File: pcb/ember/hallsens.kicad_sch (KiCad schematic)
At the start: 68 parts, among them IC1 CD4051BM96, IC2 CD4051BM96, IC3 CD4051BM96, IC4 CD4051BM96, U10 Hall_Sensor, U11 Hall_Sensor, U12 Hall_Sensor, U13 Hall_Sensor, U14 Hall_Sensor, U15 Hall_Sensor, U16 Hall_Sensor, U17 Hall_Sensor, U18 Hall_Sensor, U19 Hall_Sensor, U2 Hall_Sensor, U20 Hall_Sensor, U21 Hall_Sensor, U22 Hall_Sensor, U23 Hall_Sensor, U24 Hall_Sensor, U25 Hall_Sensor, U26 Hall_Sensor, U27 Hall_Sensor, U28 Hall_Sensor, U29 Hall_Sensor, U3 Hall_Sensor, U30 Hall_Sensor, U31 Hall_Sensor, U32 Hall_Sensor, U33 Hall_Sensor, U4 Hall_Sensor, U5 Hall_Sensor, U6 Hall_Sensor, U7 Hall_Sensor, U8 Hall_Sensor, U9 Hall_Sensor

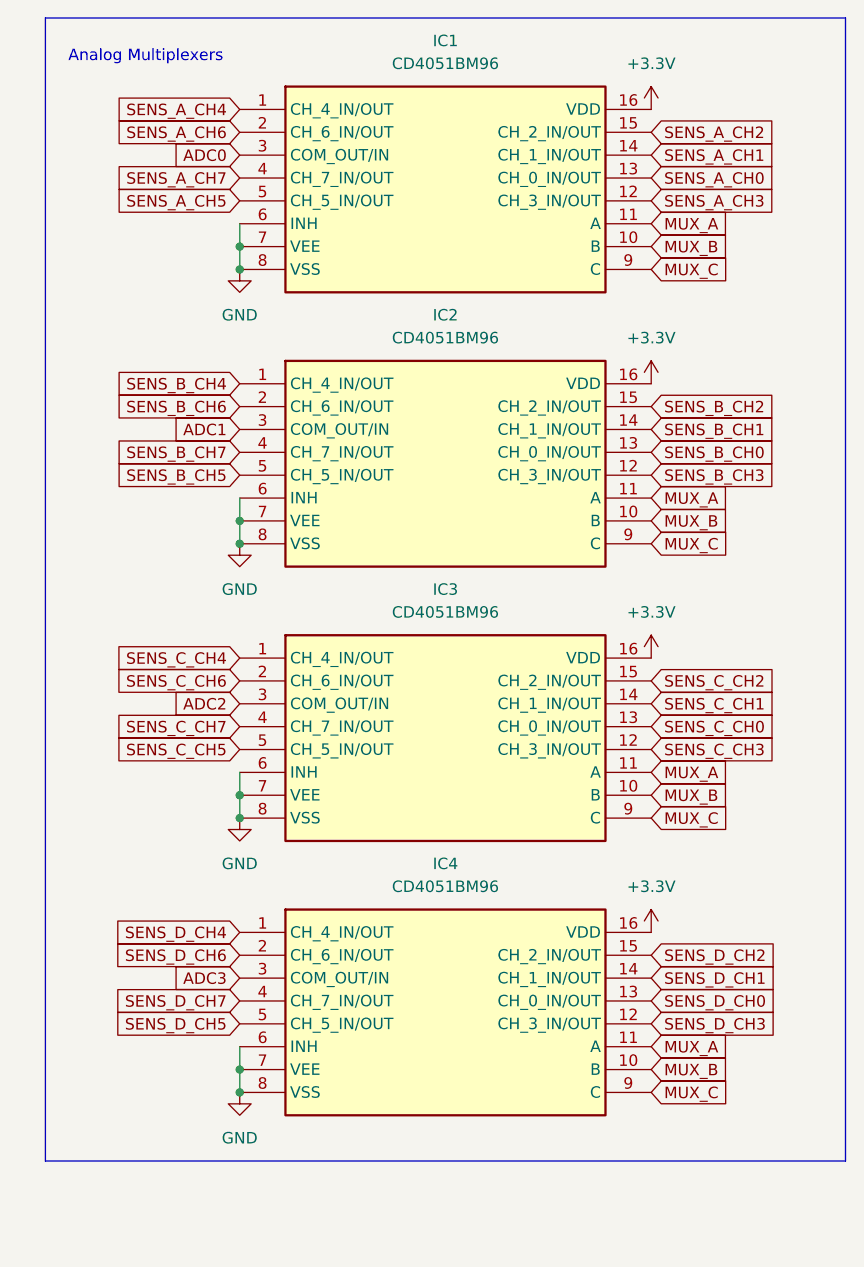
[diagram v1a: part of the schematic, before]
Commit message: :sparkles: add eeprom
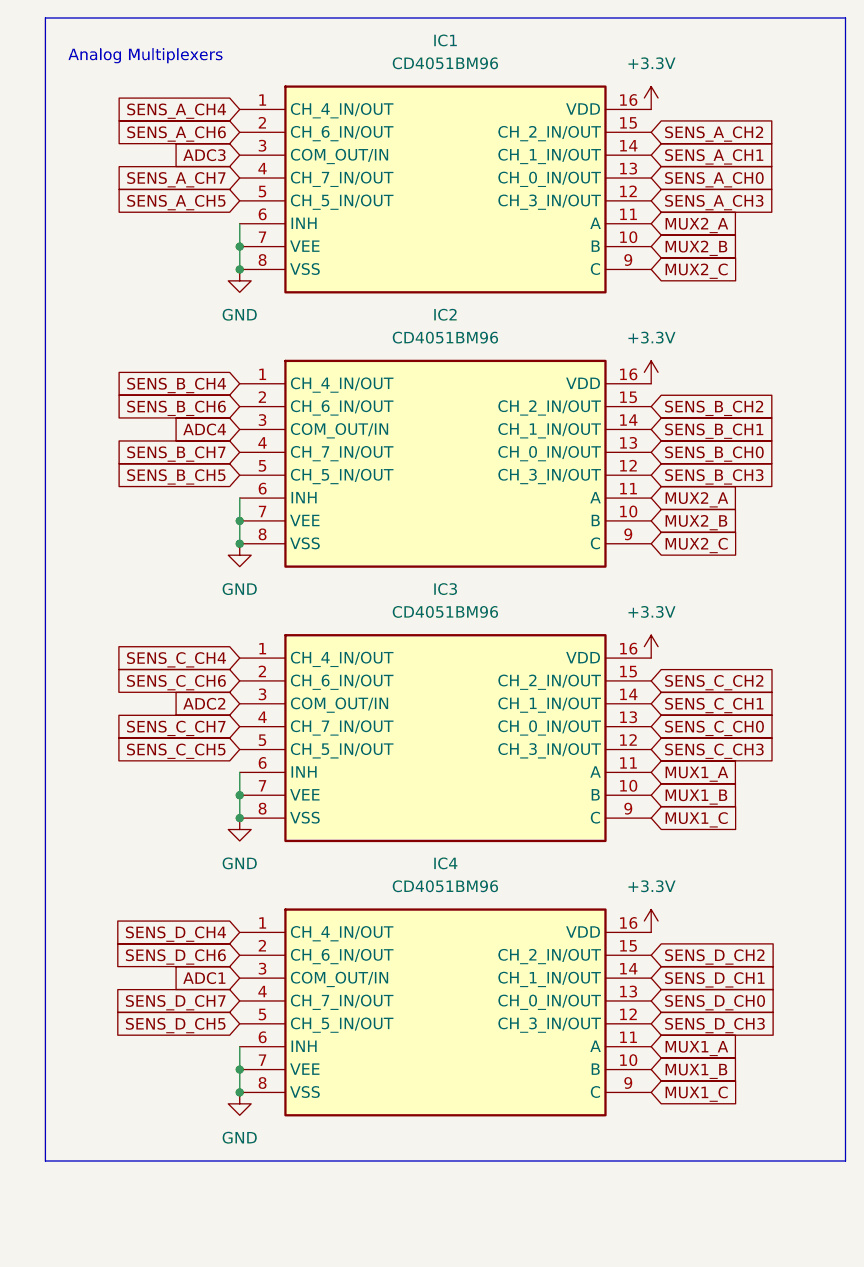
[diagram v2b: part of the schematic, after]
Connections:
- net ADC0 is gone; now on net ADC3: IC1.3 (COM_OUT/IN)
- net ADC1: now also IC4.3 (COM_OUT/IN); no longer IC2.3 (COM_OUT/IN)
- net ADC3: no longer IC4.3 (COM_OUT/IN)
- net MUX_A renamed MUX1_A
- net MUX1_A: no longer IC1.11 (A), IC2.11 (A)
- net MUX_B renamed MUX1_B
- net MUX1_B: no longer IC1.10 (B), IC2.10 (B)
- net MUX_C renamed MUX1_C
- net MUX1_C: no longer IC1.9 (C), IC2.9 (C)
- new net ADC4: IC2.3 (COM_OUT/IN)
- new net MUX2_A: IC1.11 (A), IC2.11 (A)
- new net MUX2_B: IC1.10 (B), IC2.10 (B)
- new net MUX2_C: IC1.9 (C), IC2.9 (C)
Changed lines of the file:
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@@
     )
   )
-  (global_label "MUX_C" (shape input) (at 237.49 114.3 0) (fields_autoplaced)
-    (effects (font (size 1.27 1.27)) (justify left))
-    (property "Intersheetrefs" "${INTERSHEET_REFS}" (at 246.7042 114.3 0)
-      (effects (font (size 1.27 1.27)) (justify left) hide)
-    )
-  )
-  (global_label "MUX_C" (shape input) (at 237.49 53.34 0) (fields_autoplaced)
-    (effects (font (size 1.27 1.27)) (justify left))
-    (property "Intersheetrefs" "${INTERSHEET_REFS}" (at 246.7042 53.34 0)
+  (global_label "MUX1_A" (shape input) (at 237.49 139.7 0) (fields_autoplaced)
+    (effects (font (size 1.27 1.27)) (justify left))
+    (property "Intersheetrefs" "${INTERSHEET_REFS}" (at 247.7323 139.7 0)
+      (effects (font (size 1.27 1.27)) (justify left) hide)
+    )
+  )
+  (global_label "MUX1_B" (shape input) (at 237.49 142.24 0) (fields_autoplaced)
+    (effects (font (size 1.27 1.27)) (justify left))
+    (property "Intersheetrefs" "${INTERSHEET_REFS}" (at 247.9137 142.24 0)
+      (effects (font (size 1.27 1.27)) (justify left) hide)
+    )
+  )
+  (global_label "MUX1_C" (shape input) (at 237.49 114.3 0) (fields_autoplaced)
+    (effects (font (size 1.27 1.27)) (justify left))
+    (property "Intersheetrefs" "${INTERSHEET_REFS}" (at 247.9137 114.3 0)
+      (effects (font (size 1.27 1.27)) (justify left) hide)
+    )
+  )
+  (global_label "MUX2_C" (shape input) (at 237.49 53.34 0) (fields_autoplaced)
+    (effects (font (size 1.27 1.27)) (justify left))
+    (property "Intersheetrefs" "${INTERSHEET_REFS}" (at 247.9137 53.34 0)
       (effects (font (size 1.27 1.27)) (justify left) hide)
     )
@@
     )
   )
-  (global_label "MUX_A" (shape input) (at 237.49 109.22 0) (fields_autoplaced)
-    (effects (font (size 1.27 1.27)) (justify left))
-    (property "Intersheetrefs" "${INTERSHEET_REFS}" (at 246.5228 109.22 0)
-      (effects (font (size 1.27 1.27)) (justify left) hide)
-    )
-  )
-  (global_label "MUX_B" (shape input) (at 237.49 81.28 0) (fields_autoplaced)
-    (effects (font (size 1.27 1.27)) (justify left))
-    (property "Intersheetrefs" "${INTERSHEET_REFS}" (at 246.7042 81.28 0)
+  (global_label "MUX1_A" (shape input) (at 237.49 109.22 0) (fields_autoplaced)
+    (effects (font (size 1.27 1.27)) (justify left))
+    (property "Intersheetrefs" "${INTERSHEET_REFS}" (at 247.7323 109.22 0)
       (effects (font (size 1.27 1.27)) (justify left) hide)
     )
@@
     )
   )
+  (global_label "MUX1_C" (shape input) (at 237.49 144.78 0) (fields_autoplaced)
+    (effects (font (size 1.27 1.27)) (justify left))
+    (property "Intersheetrefs" "${INTERSHEET_REFS}" (at 247.9137 144.78 0)
+      (effects (font (size 1.27 1.27)) (justify left) hide)
+    )
+  )
   (global_label "SENS_C_CH3" (shape input) (at 147.32 104.14 270) (fields_autoplaced)
     (effects (font (size 1.27 1.27)) (justify right))
@@
     )
   )
-  (global_label "ADC3" (shape input) (at 191.77 132.08 180) (fields_autoplaced)
+  (global_label "ADC1" (shape input) (at 191.77 132.08 180) (fields_autoplaced)
     (effects (font (size 1.27 1.27)) (justify right))
     (property "Intersheetrefs" "${INTERSHEET_REFS}" (at 183.9467 132.08 0)
@@
     )
   )
-  (global_label "MUX_C" (shape input) (at 237.49 83.82 0) (fields_autoplaced)
-    (effects (font (size 1.27 1.27)) (justify left))
-    (property "Intersheetrefs" "${INTERSHEET_REFS}" (at 246.7042 83.82 0)
-      (effects (font (size 1.27 1.27)) (justify left) hide)
-    )
-  )
   (global_label "SENS_A_CH0" (shape input) (at 237.49 43.18 0) (fields_autoplaced)
     (effects (font (size 1.27 1.27)) (justify left))
@@
     )
   )
-  (global_label "ADC1" (shape input) (at 191.77 71.12 180) (fields_autoplaced)
+  (global_label "ADC4" (shape input) (at 191.77 71.12 180) (fields_autoplaced)
     (effects (font (size 1.27 1.27)) (justify right))
     (property "Intersheetrefs" "${INTERSHEET_REFS}" (at 183.9467 71.12 0)
@@
     )
   )
-  (global_label "ADC0" (shape input) (at 191.77 40.64 180) (fields_autoplaced)
+  (global_label "ADC3" (shape input) (at 191.77 40.64 180) (fields_autoplaced)
     (effects (font (size 1.27 1.27)) (justify right))
     (property "Intersheetrefs" "${INTERSHEET_REFS}" (at 183.9467 40.64 0)
@@
     )
   )
-  (global_label "MUX_A" (shape input) (at 237.49 78.74 0) (fields_autoplaced)
-    (effects (font (size 1.27 1.27)) (justify left))
-    (property "Intersheetrefs" "${INTERSHEET_REFS}" (at 246.5228 78.74 0)
+  (global_label "MUX2_A" (shape input) (at 237.49 78.74 0) (fields_autoplaced)
+    (effects (font (size 1.27 1.27)) (justify left))
+    (property "Intersheetrefs" "${INTERSHEET_REFS}" (at 247.7323 78.74 0)
       (effects (font (size 1.27 1.27)) (justify left) hide)
     )
@@
     )
   )
-  (global_label "MUX_B" (shape input) (at 237.49 142.24 0) (fields_autoplaced)
-    (effects (font (size 1.27 1.27)) (justify left))
-    (property "Intersheetrefs" "${INTERSHEET_REFS}" (at 246.7042 142.24 0)
+  (global_label "MUX2_B" (shape input) (at 237.49 81.28 0) (fields_autoplaced)
+    (effects (font (size 1.27 1.27)) (justify left))
+    (property "Intersheetrefs" "${INTERSHEET_REFS}" (at 247.9137 81.28 0)
       (effects (font (size 1.27 1.27)) (justify left) hide)
     )
@@
     )
   )
-  (global_label "MUX_A" (shape input) (at 237.49 139.7 0) (fields_autoplaced)
-    (effects (font (size 1.27 1.27)) (justify left))
-    (property "Intersheetrefs" "${INTERSHEET_REFS}" (at 246.5228 139.7 0)
+  (global_label "MUX2_C" (shape input) (at 237.49 83.82 0) (fields_autoplaced)
+    (effects (font (size 1.27 1.27)) (justify left))
+    (property "Intersheetrefs" "${INTERSHEET_REFS}" (at 247.9137 83.82 0)
       (effects (font (size 1.27 1.27)) (justify left) hide)
     )
@@
     )
   )
-  (global_label "MUX_B" (shape input) (at 237.49 50.8 0) (fields_autoplaced)
-    (effects (font (size 1.27 1.27)) (justify left))
-    (property "Intersheetrefs" "${INTERSHEET_REFS}" (at 246.7042 50.8 0)
+  (global_label "MUX2_B" (shape input) (at 237.49 50.8 0) (fields_autoplaced)
+    (effects (font (size 1.27 1.27)) (justify left))
+    (property "Intersheetrefs" "${INTERSHEET_REFS}" (at 247.9137 50.8 0)
       (effects (font (size 1.27 1.27)) (justify left) hide)
     )
@@
     )
   )
-  (global_label "MUX_C" (shape input) (at 237.49 144.78 0) (fields_autoplaced)
-    (effects (font (size 1.27 1.27)) (justify left))
-    (property "Intersheetrefs" "${INTERSHEET_REFS}" (at 246.7042 144.78 0)
-      (effects (font (size 1.27 1.27)) (justify left) hide)
-    )
-  )
   (global_label "SENS_D_CH5" (shape input) (at 90.17 134.62 270) (fields_autoplaced)
     (effects (font (size 1.27 1.27)) (justify right))
@@
     )
   )
-  (global_label "MUX_A" (shape input) (at 237.49 48.26 0) (fields_autoplaced)
-    (effects (font (size 1.27 1.27)) (justify left))
-    (property "Intersheetrefs" "${INTERSHEET_REFS}" (at 246.5228 48.26 0)
+  (global_label "MUX2_A" (shape input) (at 237.49 48.26 0) (fields_autoplaced)
+    (effects (font (size 1.27 1.27)) (justify left))
+    (property "Intersheetrefs" "${INTERSHEET_REFS}" (at 247.7323 48.26 0)
       (effects (font (size 1.27 1.27)) (justify left) hide)
     )
@@
     )
   )
-  (global_label "MUX_B" (shape input) (at 237.49 111.76 0) (fields_autoplaced)
-    (effects (font (size 1.27 1.27)) (justify left))
-    (property "Intersheetrefs" "${INTERSHEET_REFS}" (at 246.7042 111.76 0)
-      (effects (font (size 1.27 1.27)) (justify left) hide)
-    )
+  (global_label "MUX1_B" (shape input) (at 237.49 111.76 0) (fields_autoplaced)
+    (effects (font (size 1.27 1.27)) (justify left))
+    (property "Intersheetrefs" "${INTERSHEET_REFS}" (at 247.9137 111.76 0)
+      (effects (font (size 1.27 1.27)) (justify left) hide)
+    )

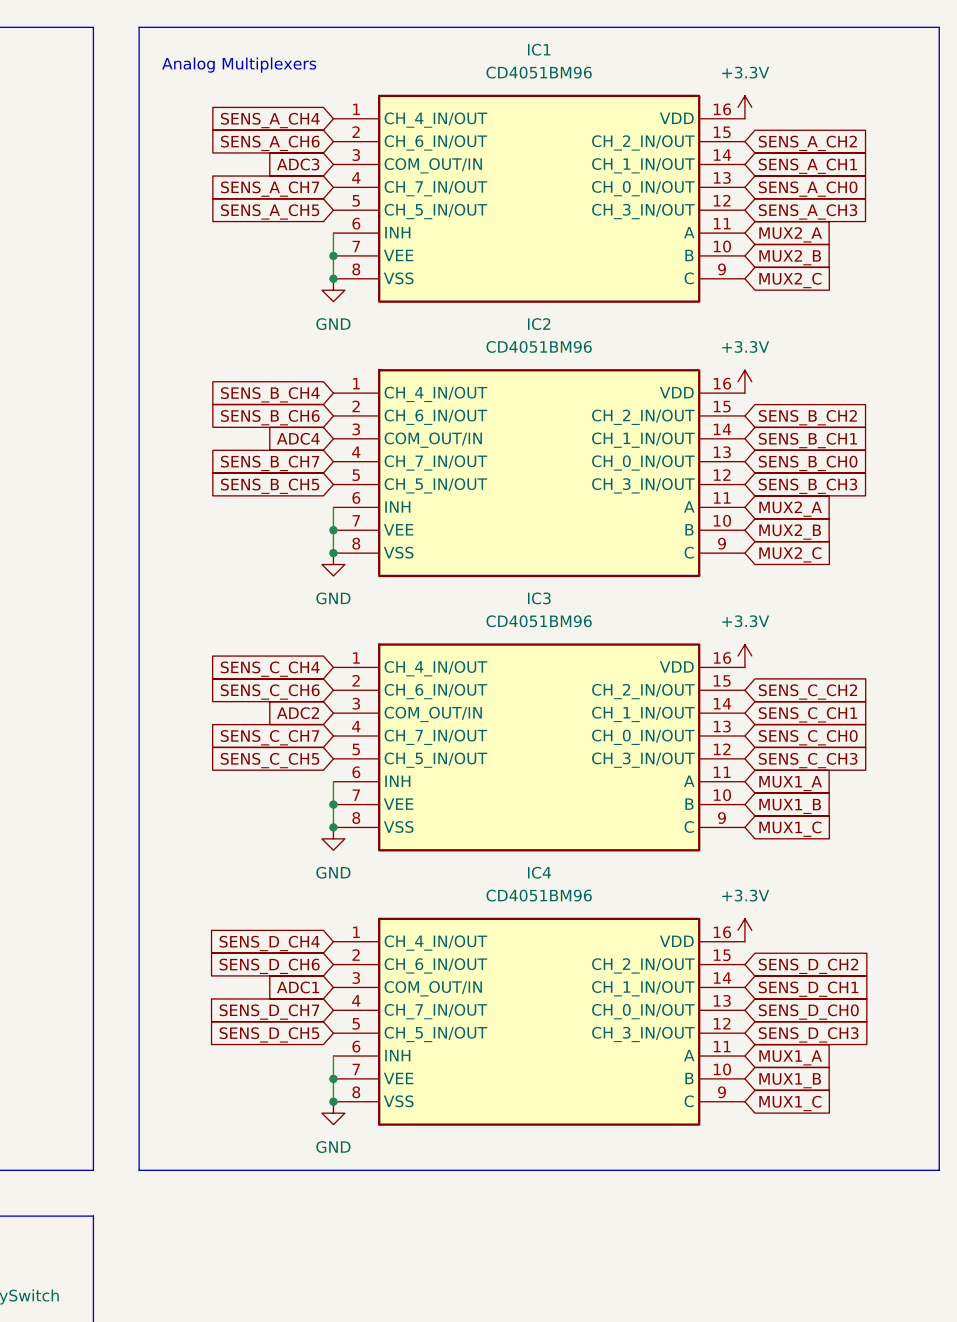
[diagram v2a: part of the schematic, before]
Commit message: :sparkles: replace cd4052->ad708
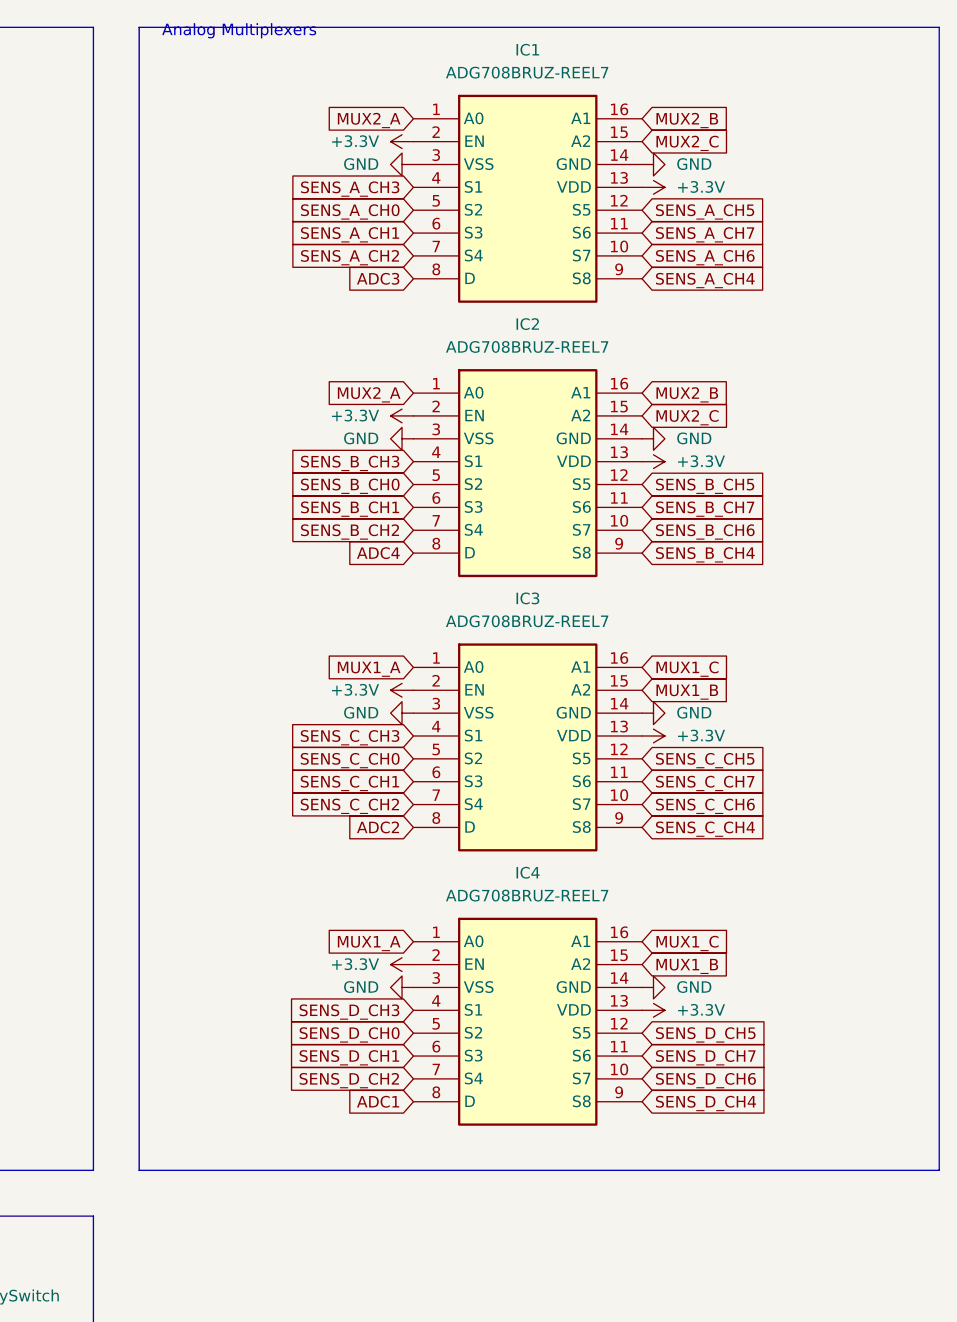
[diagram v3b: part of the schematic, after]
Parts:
- removed IC1, IC2, IC3, IC4: CD4051BM96, ember:SOIC127P600X175-16N, symbol ember_cd4051bm96:CD4051BM96
- added IC1, IC2, IC3, IC4: ADG708BRUZ-REEL7, SOP65P640X120-16N, symbol ember_adg708:ADG708BRUZ-REEL7
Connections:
- net +3.3V: now also IC1.13 (VDD), IC1.2 (EN), IC2.13 (VDD), IC2.2 (EN), IC3.13 (VDD), IC3.2 (EN), IC4.13 (VDD), IC4.2 (EN)
- net ADC1: now also IC4.8 (D)
- net ADC2: now also IC3.8 (D)
- net ADC3: now also IC1.8 (D)
- net ADC4: now also IC2.8 (D)
- net GND: now also IC1.14 (GND), IC1.3 (VSS), IC2.14 (GND), IC2.3 (VSS), IC3.14 (GND), IC3.3 (VSS), IC4.14 (GND), IC4.3 (VSS)
- net MUX1_A: now also IC3.1 (A0), IC4.1 (A0)
- net MUX1_B: now also IC3.15 (A2), IC4.15 (A2)
- net MUX1_C: now also IC3.16 (A1), IC4.16 (A1)
- net MUX2_A: now also IC1.1 (A0), IC2.1 (A0)
- net MUX2_B: now also IC1.16 (A1), IC2.16 (A1)
- net MUX2_C: now also IC1.15 (A2), IC2.15 (A2)
- net SENS_A_CH0: now also IC1.5 (S2)
- net SENS_A_CH1: now also IC1.6 (S3)
- net SENS_A_CH2: now also IC1.7 (S4)
- net SENS_A_CH3: now also IC1.4 (S1)
- net SENS_A_CH4: now also IC1.9 (S8)
- net SENS_A_CH5: now also IC1.12 (S5)
- net SENS_A_CH6: now also IC1.10 (S7)
- net SENS_A_CH7: now also IC1.11 (S6)
- net SENS_B_CH0: now also IC2.5 (S2)
- net SENS_B_CH1: now also IC2.6 (S3)
- net SENS_B_CH2: now also IC2.7 (S4)
- net SENS_B_CH3: now also IC2.4 (S1)
- net SENS_B_CH4: now also IC2.9 (S8)
- net SENS_B_CH5: now also IC2.12 (S5)
- net SENS_B_CH6: now also IC2.10 (S7)
- net SENS_B_CH7: now also IC2.11 (S6)
- net SENS_C_CH0: now also IC3.5 (S2)
- net SENS_C_CH1: now also IC3.6 (S3)
- net SENS_C_CH2: now also IC3.7 (S4)
- net SENS_C_CH3: now also IC3.4 (S1)
- net SENS_C_CH4: now also IC3.9 (S8)
- net SENS_C_CH5: now also IC3.12 (S5)
- net SENS_C_CH6: now also IC3.10 (S7)
- net SENS_C_CH7: now also IC3.11 (S6)
- net SENS_D_CH0: now also IC4.5 (S2)
- net SENS_D_CH1: now also IC4.6 (S3)
- net SENS_D_CH2: now also IC4.7 (S4)
- net SENS_D_CH3: now also IC4.4 (S1)
- net SENS_D_CH4: now also IC4.9 (S8)
- net SENS_D_CH5: now also IC4.12 (S5)
- net SENS_D_CH6: now also IC4.10 (S7)
- net SENS_D_CH7: now also IC4.11 (S6)
